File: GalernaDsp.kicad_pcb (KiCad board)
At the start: 2 copper layers, 2.2 x 9.4 mm, 119 parts, among them CN100 HX JN1.27-2X5 TP H4.9, J100 DM3CS-SF, J200 Headphones, J201 AudioInput, J202 AudioOutput, J300 USB_C_Receptacle_USB2.0_16P, SW400 100SP1T1B4M2QE, SW401 100SP1T1B4M2QE, U100 SW_RUN, U101 STM32F405RGTx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

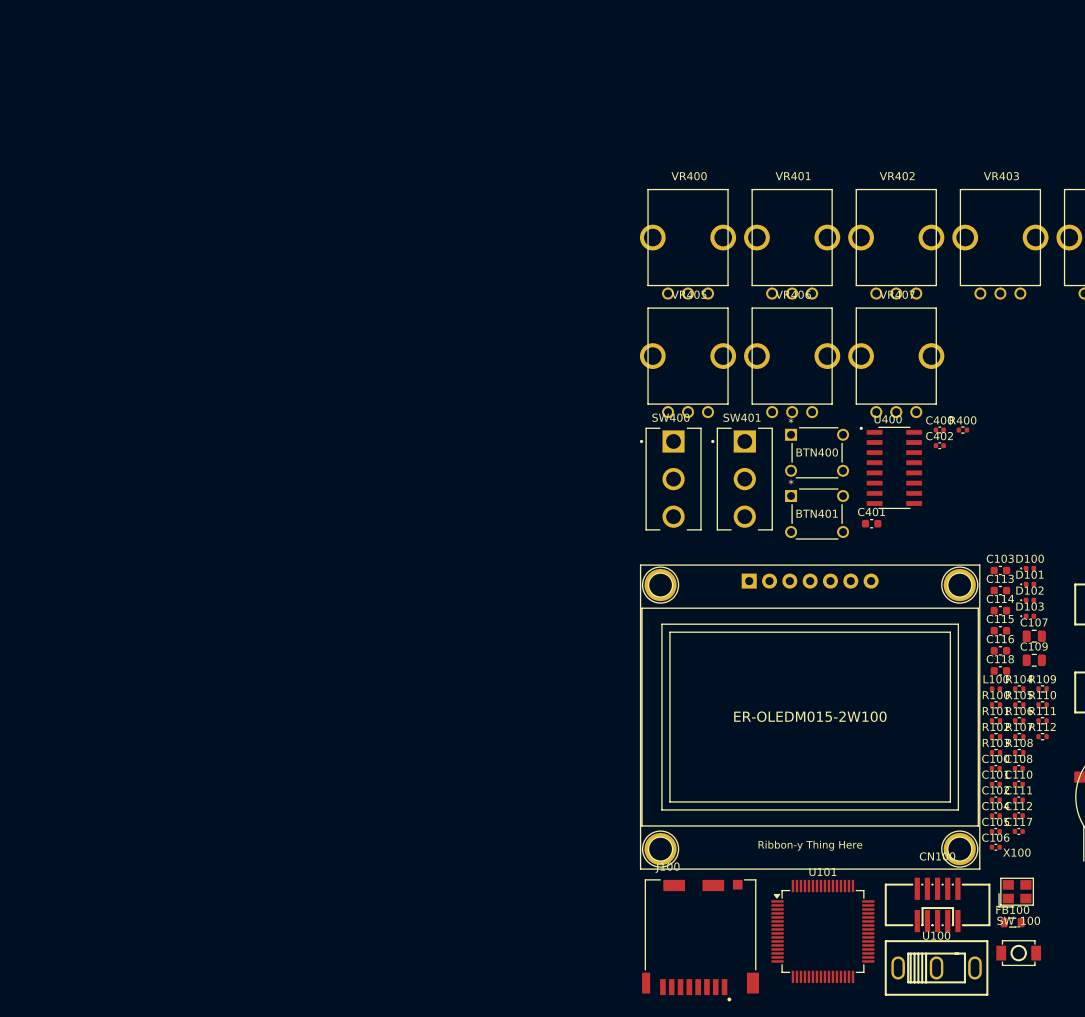
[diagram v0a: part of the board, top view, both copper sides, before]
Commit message: decoupling caps route
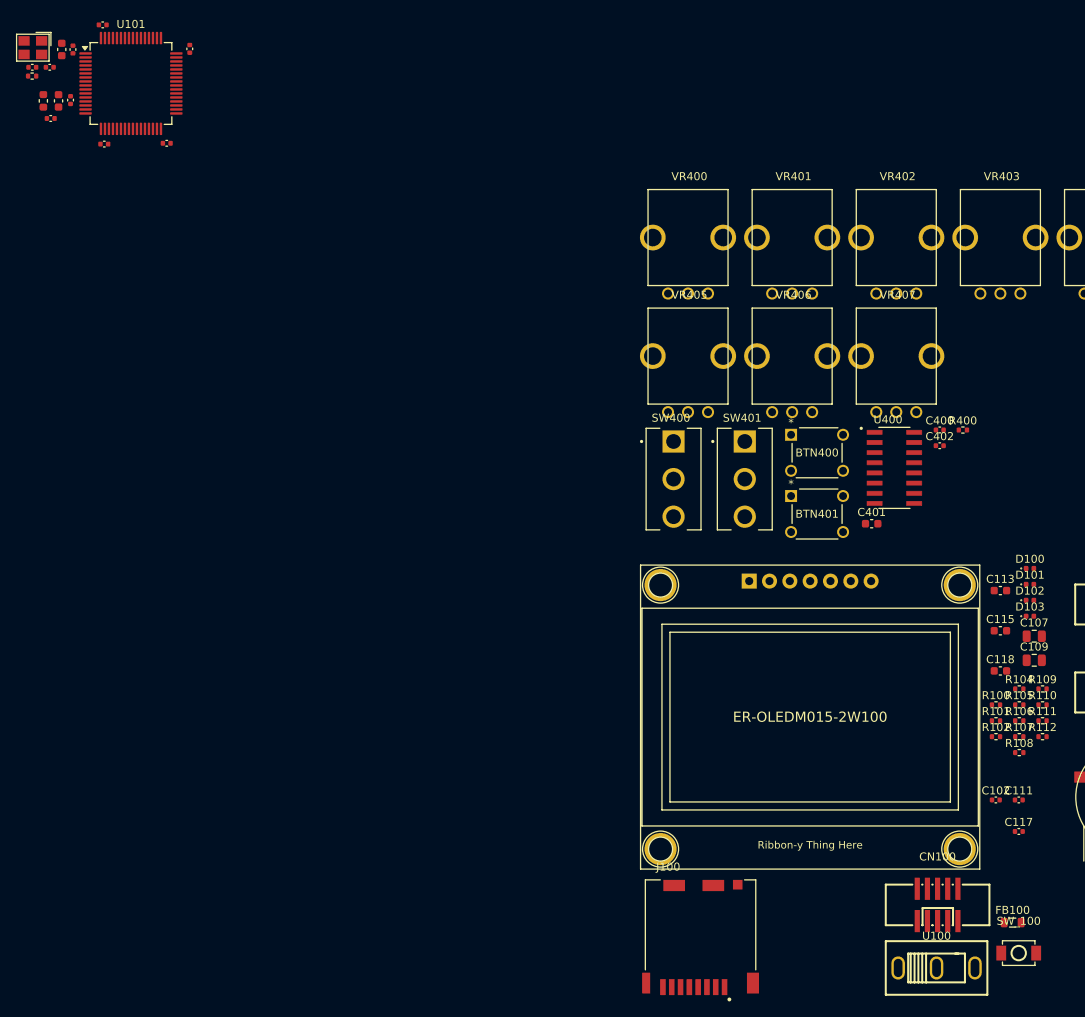
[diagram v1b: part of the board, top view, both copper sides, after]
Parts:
- C116: footprint Capacitor_SMD:C_0603_1608Metric -> Capacitor_SMD:C_0402_1005Metric
- L100: footprint Inductor_SMD:L_0402_1005Metric -> Inductor_SMD:L_0603_1608Metric
- moved X100 162.1 mm to (25.0, 23.4), turned to 180 degrees
- moved C101 150.1 mm to (24.9, 25.8)
- moved C104 149.9 mm to (30.0, 23.6), turned to 90 degrees
- moved C110 148.7 mm to (33.7, 20.5)
- moved C112 148.5 mm to (29.7, 29.9), turned to 90 degrees
- moved C100 147.2 mm to (27.1, 25.8), turned to 180 degrees
- moved R103 147.2 mm to (24.9, 26.9)
- moved C105 140.7 mm to (33.9, 35.4), turned to 180 degrees
- moved L100 139.9 mm to (26.3, 30.0), turned to 90 degrees
- moved C108 137.2 mm to (44.6, 23.5), turned to 90 degrees
- moved U101 136.8 mm to (37.2, 27.8)
- moved C116 136.1 mm to (27.2, 32.2)
- moved C106 136.0 mm to (41.7, 35.3)
- moved C103 134.2 mm to (28.6, 23.6), turned to 90 degrees
- moved C114 133.9 mm to (28.2, 30.0), turned to 90 degrees
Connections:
- net /[3]Input Control/POT_0_CTL renamed /[3] Input Control/POT_0_CTL
- net /[3]Input Control/POT_1_CTL renamed /[3] Input Control/POT_1_CTL
- net /[3]Input Control/POT_2_CTL renamed /[3] Input Control/POT_2_CTL
- net /[3]Input Control/POT_3_CTL renamed /[3] Input Control/POT_3_CTL
- net /[3]Input Control/POT_4_CTL renamed /[3] Input Control/POT_4_CTL
- net /[3]Input Control/POT_5_CTL renamed /[3] Input Control/POT_5_CTL
- net /[3]Input Control/POT_6_CTL renamed /[3] Input Control/POT_6_CTL
- net /[3]Input Control/POT_7_CTL renamed /[3] Input Control/POT_7_CTL
- U101 pad 1: GND -> +3V3
- U101 pad 19: GND -> +3V3
- U101 pad 32: GND -> +3V3
- U101 pad 48: GND -> +3V3
- U101 pad 64: GND -> +3V3

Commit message: constraints updated
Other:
- rule pad_to_mask_clearance: 0 -> 0.1
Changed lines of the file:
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@@
 	)
 	(setup
-		(pad_to_mask_clearance 0)
+		(stackup
+			(layer "F.SilkS"
+				(type "Top Silk Screen")
+			)
+			(layer "F.Paste"
+				(type "Top Solder Paste")
+			)
+			(layer "F.Mask"
+				(type "Top Solder Mask")
+				(thickness 0.01)
+			)
+			(layer "F.Cu"
+				(type "copper")
+				(thickness 0.035)
+			)
+			(layer "dielectric 1"
+				(type "core")
+				(thickness 1.51)
+				(material "FR4")
+				(epsilon_r 4.5)
+				(loss_tangent 0.02)
+			)
+			(layer "B.Cu"
+				(type "copper")
+				(thickness 0.035)
+			)
+			(layer "B.Mask"
+				(type "Bottom Solder Mask")
+				(thickness 0.01)
+			)
+			(layer "B.Paste"
+				(type "Bottom Solder Paste")
+			)
+			(layer "B.SilkS"
+				(type "Bottom Silk Screen")
+			)
+			(copper_finish "None")
+			(dielectric_constraints no)
+		)
+		(pad_to_mask_clearance 0.1)
+		(solder_mask_min_width 0.1)
 		(allow_soldermask_bridges_in_footprints no)
 		(tenting front back)

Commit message: rules updated
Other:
- copper layers 2 -> 4
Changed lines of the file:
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@@
 	(generator_version "9.0")
 	(general
-		(thickness 1.6)
+		(thickness 1.726)
 		(legacy_teardrops no)
 	)
@@
 	(layers
 		(0 "F.Cu" signal)
+		(4 "In1.Cu" power)
+		(6 "In2.Cu" power)
 		(2 "B.Cu" signal)
-		(9 "F.Adhes" user "F.Adhesive")
-		(11 "B.Adhes" user "B.Adhesive")
 		(13 "F.Paste" user)
 		(15 "B.Paste" user)
@@
 		(1 "F.Mask" user)
 		(3 "B.Mask" user)
-		(17 "Dwgs.User" user "User.Drawings")
-		(19 "Cmts.User" user "User.Comments")
-		(21 "Eco1.User" user "User.Eco1")
-		(23 "Eco2.User" user "User.Eco2")
 		(25 "Edge.Cuts" user)
 		(27 "Margin" user)
 		(31 "F.CrtYd" user "F.Courtyard")
 		(29 "B.CrtYd" user "B.Courtyard")
-		(35 "F.Fab" user)
-		(33 "B.Fab" user)
-		(39 "User.1" user)
-		(41 "User.2" user)
-		(43 "User.3" user)
-		(45 "User.4" user)
 	)
 	(setup
@@
 			(layer "F.Mask"
 				(type "Top Solder Mask")
+				(color "Black")
 				(thickness 0.01)
 			)
@@
 			)
 			(layer "dielectric 1"
+				(type "prepreg")
+				(thickness 0.2)
+				(material "FR4")
+				(epsilon_r 4.5)
+				(loss_tangent 0.02)
+			)
+			(layer "In1.Cu"
+				(type "copper")
+				(thickness 0.018)
+			)
+			(layer "dielectric 2"
 				(type "core")
-				(thickness 1.51)
+				(thickness 1.2)
+				(material "FR4")
+				(epsilon_r 4.5)
+				(loss_tangent 0.02)
+			)
+			(layer "In2.Cu"
+				(type "copper")
+				(thickness 0.018)
+			)
+			(layer "dielectric 3"
+				(type "prepreg")
+				(thickness 0.2)
 				(material "FR4")
 				(epsilon_r 4.5)
@@
 			(layer "B.Mask"
 				(type "Bottom Solder Mask")
+				(color "Black")
 				(thickness 0.01)
 			)

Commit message: codec placed
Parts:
- C212, C213: footprint Capacitor_SMD:C_0603_1608Metric -> Galerna:CHEMI-F80
- L300: footprint Inductor_SMD:L_0603_1608Metric -> Inductor_SMD:L_0805_2012Metric
- moved C106 202.3 mm to (242.6, 59.5)
- moved C105 201.5 mm to (233.8, 60.6)
- moved C112 201.5 mm to (229.6, 55.1)
- moved C114 201.5 mm to (228.1, 55.2)
- moved X100 201.5 mm to (224.9, 48.5)
- moved C103 201.5 mm to (228.5, 48.7)
- moved C104 201.5 mm to (229.9, 48.8)
- moved C110 201.5 mm to (233.6, 45.7)
- moved C116 201.5 mm to (227.1, 57.4)
- moved L100 201.5 mm to (226.2, 55.2)
- moved U101 201.5 mm to (237.2, 53.0)
- moved C100 200.9 mm to (226.4, 51.0)
- moved R103 200.6 mm to (223.9, 52.1)
- moved C101 200.6 mm to (223.9, 51.0)
- moved C108 200.0 mm to (243.1, 47.5)
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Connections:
- U101 pad 10: I2S_SDI -> unconnected-(U101-PC2-Pad10)
- U101 pad 11: I2S_SD -> unconnected-(U101-PC3-Pad11)
- U101 pad 29: I2S_CK -> I2C_SCL
- U101 pad 30: unconnected-(U101-PB11-Pad30) -> I2C_SDA
- U101 pad 34: unconnected-(U101-PB13-Pad34) -> I2S_CK
- U101 pad 35: unconnected-(U101-PB14-Pad35) -> I2S_SDI
- U101 pad 36: unconnected-(U101-PB15-Pad36) -> I2S_SD
- U101 pad 58: I2S_SCL -> unconnected-(U101-PB6-Pad58)
- U101 pad 59: I2S_SCA -> unconnected-(U101-PB7-Pad59)
- U200 pad 23: I2S_SCA -> I2C_SDA
- U200 pad 24: I2S_SCL -> I2C_SCL
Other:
- board size 2.2 x 9.4 mm -> 191.5 x 124.5 mm

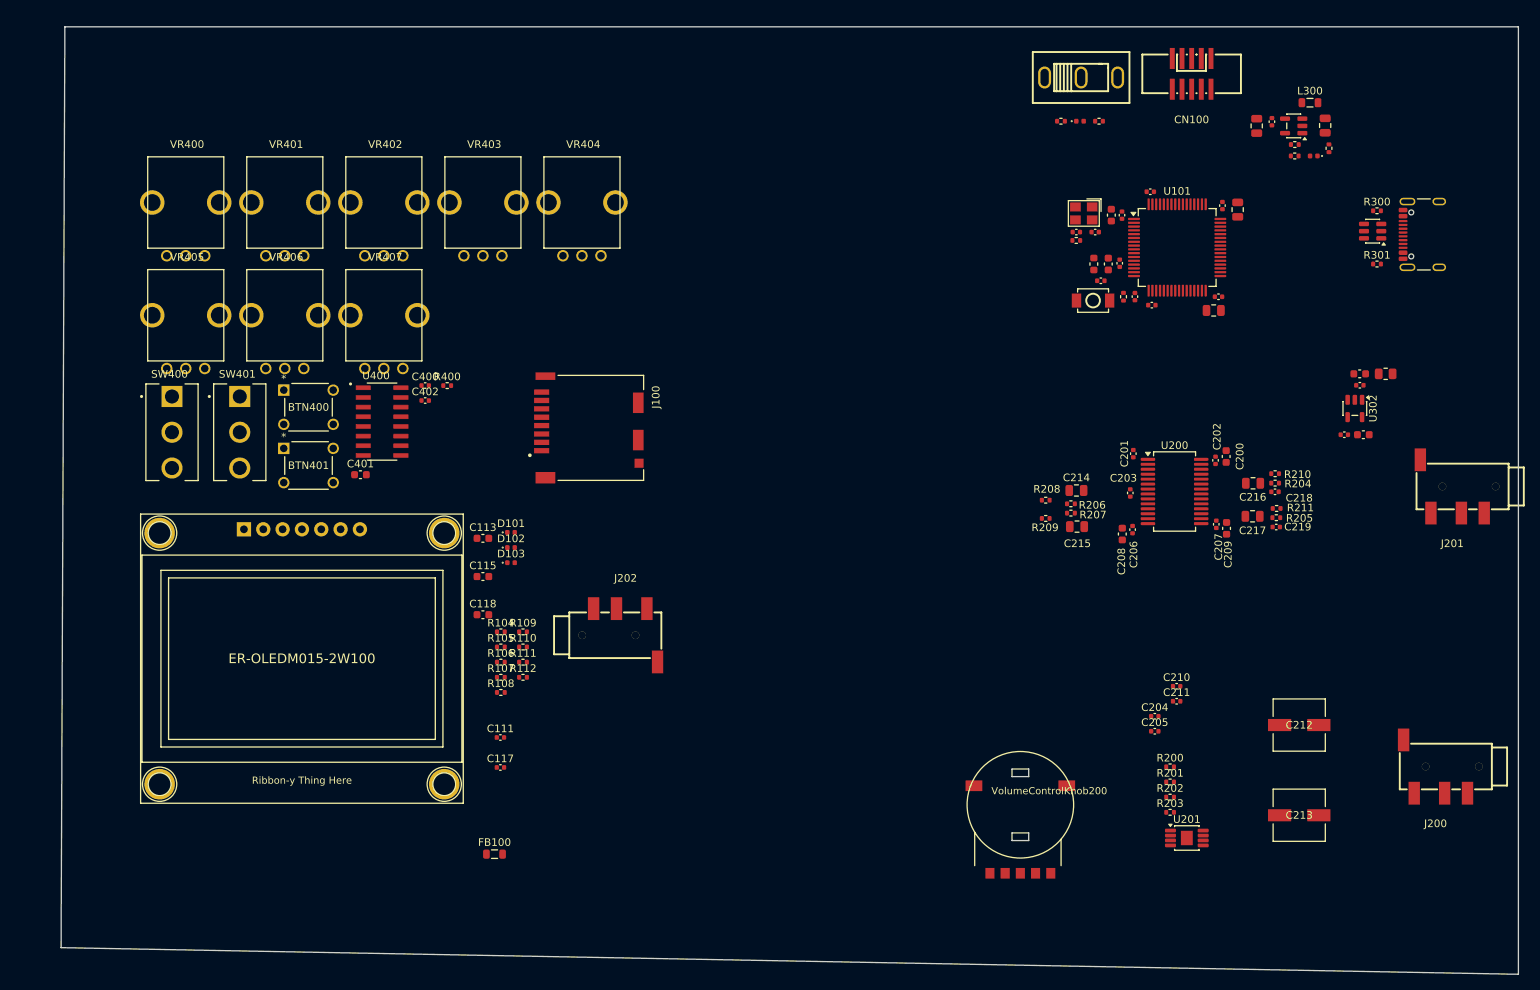
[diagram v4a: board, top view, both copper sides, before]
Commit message: edge cuts with rectangle
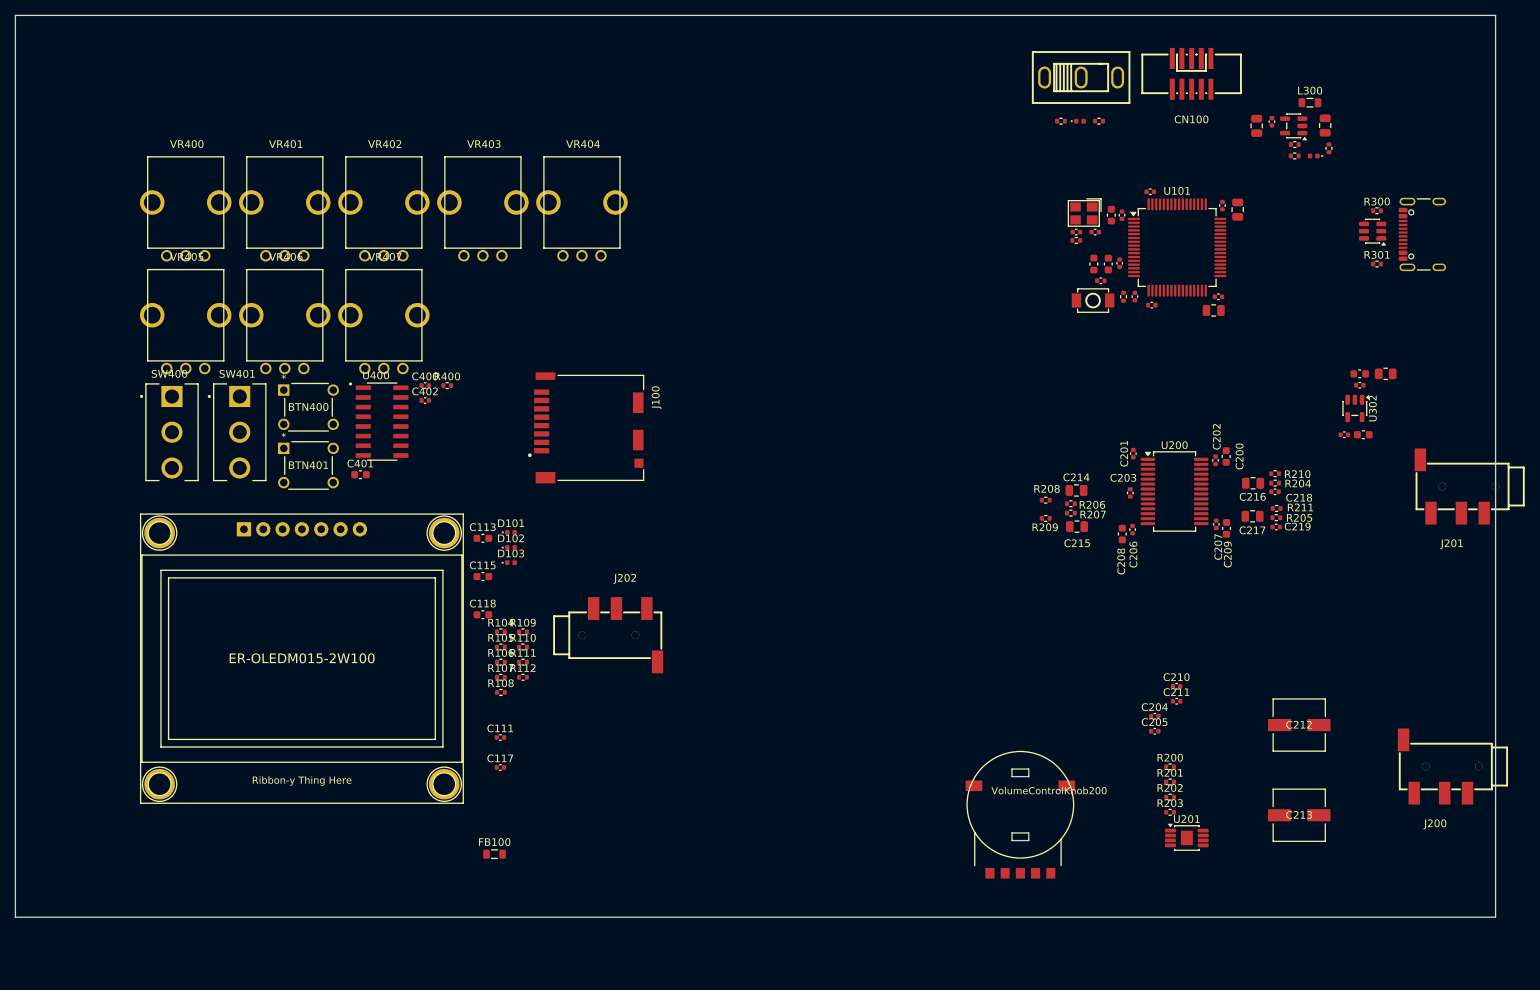
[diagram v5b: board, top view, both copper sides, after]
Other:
- board size 191.5 x 124.5 mm -> 194.5 x 118.5 mm
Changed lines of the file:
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@@
 		)
 	)
-	(gr_line
-		(start 282 24)
-		(end 282 148.5)
+	(gr_rect
+		(start 84.5 22.5)
+		(end 279 141)
 		(stroke
 			(width 0.05)
 			(type default)
 		)
+		(fill no)
 		(layer "Edge.Cuts")
 	)
-	(gr_line
-		(start 90.5 145)
-		(end 91 24)
-		(stroke
-			(width 0.05)
-			(type default)
-		)
-		(layer "Edge.Cuts")
-	)
-	(gr_line
-		(start 91 24)
-		(end 282 24)
-		(stroke
-			(width 0.05)
-			(type default)
-		)
-		(layer "Edge.Cuts")
-	)
-	(gr_line
-		(start 282 148.5)
-		(end 90.5 145)
-		(stroke
-			(width 0.05)
-			(type default)
-		)
-		(layer "Edge.Cuts")
-	)
